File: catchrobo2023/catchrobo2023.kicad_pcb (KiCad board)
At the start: 2 copper layers, 72 x 47 mm, 38 parts, among them J1 Conn_01x03_Male, J2 Conn_01x03_Male, J3 Conn_01x03_Male, J4 Conn_01x02_Male, J5 Conn_01x02_Male, J6 Conn_01x02_Male, J7 Conn_01x02_Male, J8 Conn_01x02_Male, Q1 AO3401A, SW1 SW_SPDT, SW2 SW_DIP_x04, U11 SPT15, U2 RaspberryPiPicoW, U3 AZ1084-5.0, U4 LBR-127HLD, U5 LBR-127HLD, U6 LBR-127HLD, U7 LBR-127HLD, U8 CD4051BM96

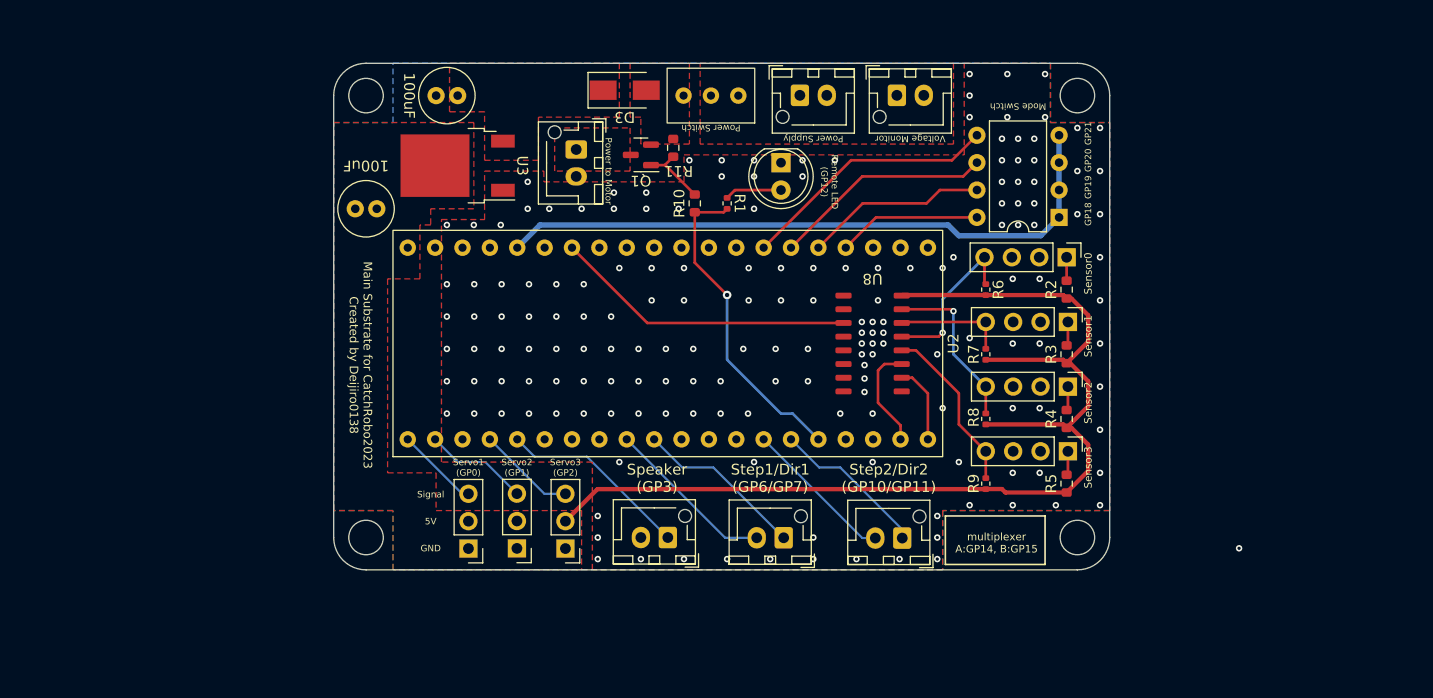
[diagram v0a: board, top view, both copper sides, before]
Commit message: 5V電源(XH)を追加
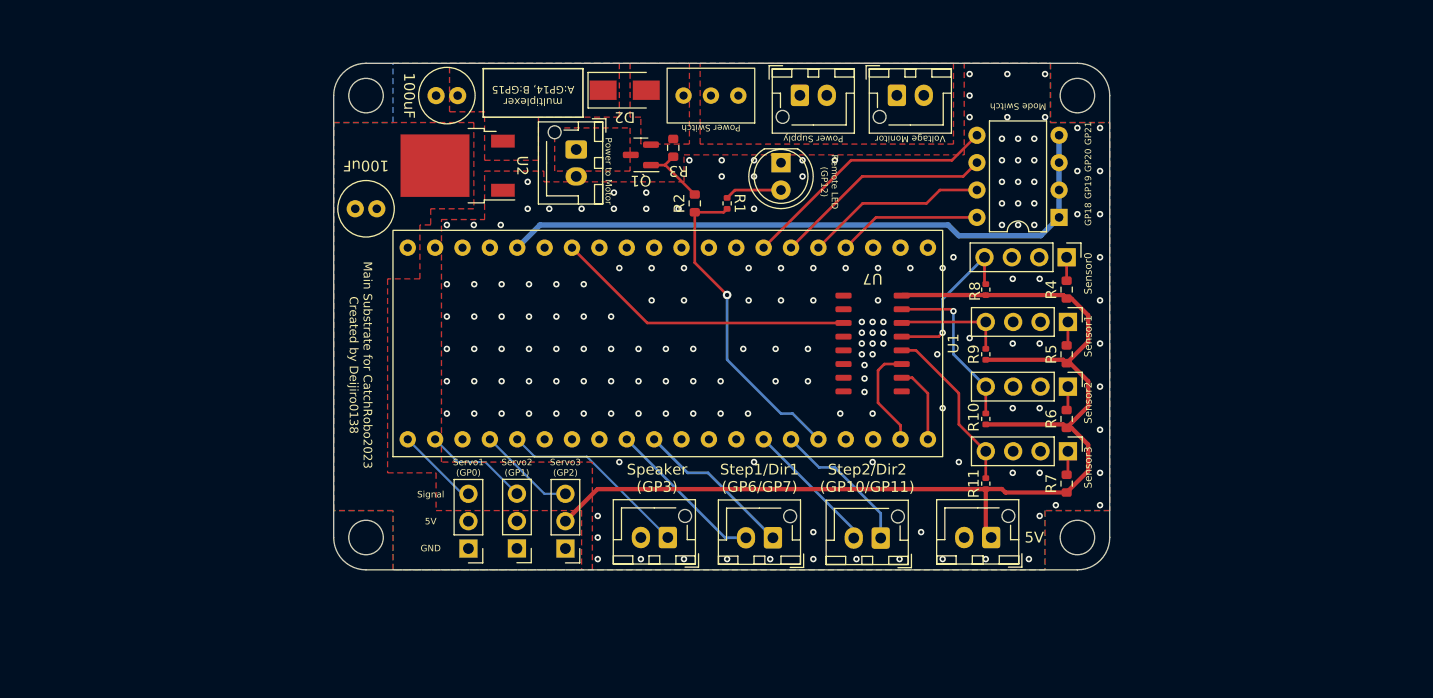
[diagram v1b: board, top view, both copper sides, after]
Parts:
- added J6: Conn_01x02_Male, Connector_JST:JST_XH_B2B-XH-AM_1x02_P2.50mm_Vertical, F.Cu at (141.0, 117.0)
- moved J5 2.00 mm to (130.8, 117.0)
- moved J4 1.00 mm to (120.8, 117.0)
- renumbered D2 to D1, D3 to D2, J4 to J1, J6 to J2, J7 to J3, J5 to J4, J8 to J5, J1 to J7, J2 to J8, J3 to J9, R8 to R10, R9 to R11, R10 to R2, R11 to R3, R2 to R4, R3 to R5, R4 to R6, R5 to R7, R6 to R8, R7 to R9, U2 to U1, U3 to U2, U4 to U3, U5 to U4, U6 to U5, U7 to U6, U8 to U7, U11 to U8
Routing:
- net +5V: track 102.3 -> 107.0 mm
- net /STEP2: track 14.2 -> 12.6 mm
- net /DIR2: track 14.6 -> 13.5 mm
- net /STEP1: track 15.8 -> 14.8 mm
- net /DIR1: track 15.8 -> 14.8 mm
- net (no net): vias 1 -> 0

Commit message: コントローラへの配線以外は完了
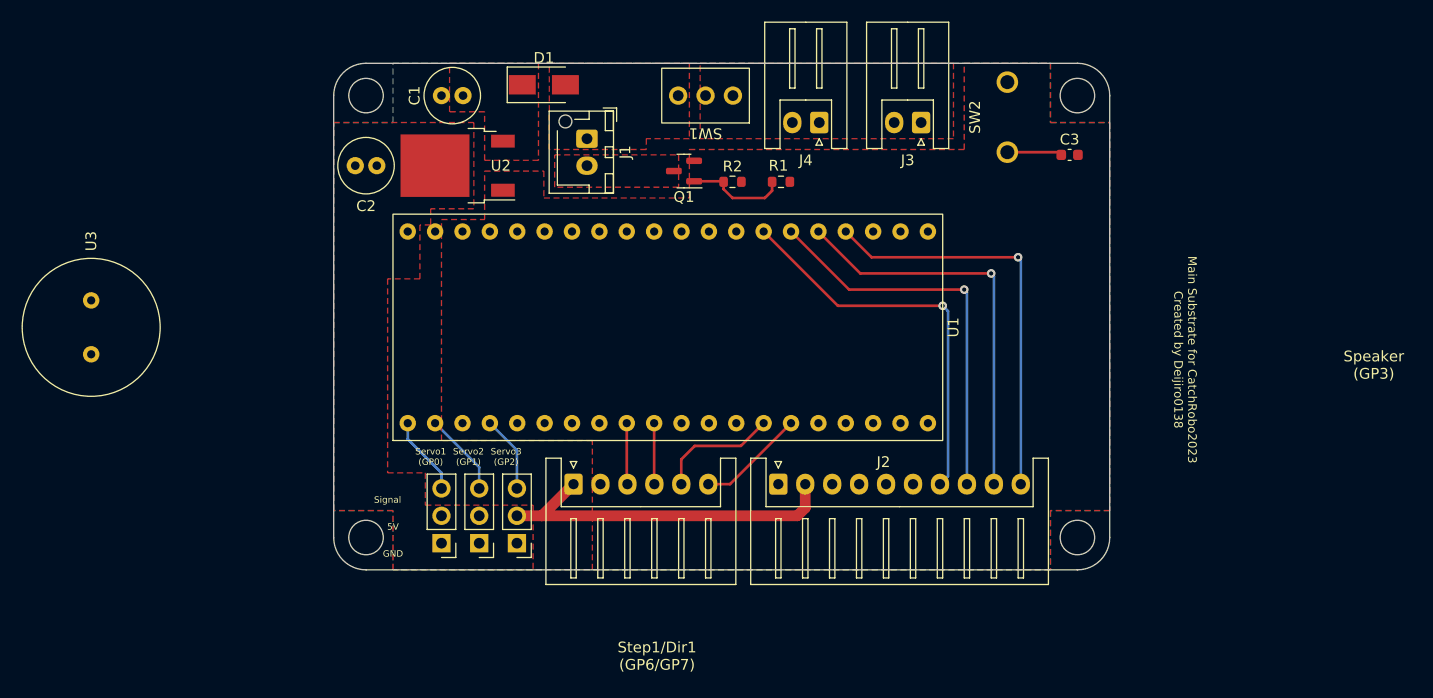
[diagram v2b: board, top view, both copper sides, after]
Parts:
- removed D2: D_Schottky, Diode_SMD:D_SMA
- removed J9: Conn_01x03_Male, Connector_PinHeader_2.54mm:PinHeader_1x03_P2.54mm_Vertical
- removed R10, R11, R8, R9: 1k, Resistor_SMD:R_0402_1005Metric
- removed R3: 10k, Resistor_SMD:R_0603_1608Metric
- removed R4, R5, R6, R7: 220, Resistor_SMD:R_0603_1608Metric
- removed U4, U5, U6: LBR-127HLD, Connector_PinHeader_2.54mm:PinHeader_1x04_P2.54mm_Vertical
- removed U7: CD4051BM96, Catchrobo_parts:SOIC-16-150mil
- removed U8: SPT15, Connector_JST:JST_XH_B2B-XH-AM_1x02_P2.50mm_Vertical
- added C3: 0.1u, Capacitor_SMD:C_0603_1608Metric, F.Cu at (148.3, 81.5)
- D1: value LED -> D_Schottky; footprint LED_THT:LED_D5.0mm -> Diode_SMD:D_SMA
- J2: value Conn_01x02_Male -> Conn_01x10_Male; footprint Connector_JST:JST_XH_B2B-XH-AM_1x02_P2.50mm_Vertical -> Connector_JST:JST_XH_S10B-XH-A_1x10_P2.50mm_Horizontal
- J3, J4: footprint Connector_JST:JST_XH_B2B-XH-AM_1x02_P2.50mm_Vertical -> Connector_JST:JST_XH_S2B-XH-A_1x02_P2.50mm_Horizontal
- J5: value Conn_01x02_Male -> Conn_01x06_Male; footprint Connector_JST:JST_XH_B2B-XH-AM_1x02_P2.50mm_Vertical -> Connector_JST:JST_XH_S6B-XH-A_1x06_P2.50mm_Horizontal
- J6: value Conn_01x02_Male -> Conn_01x03_Male; footprint Connector_JST:JST_XH_B2B-XH-AM_1x02_P2.50mm_Vertical -> Connector_PinHeader_2.54mm:PinHeader_1x03_P2.54mm_Vertical
- Q1: value AO3401A -> Q_NMOS_GSD
- R1: value 1k -> 330; footprint Resistor_SMD:R_0402_1005Metric -> Resistor_SMD:R_0603_1608Metric
- R2: value 330 -> 10k
- SW2: value SW_DIP_x04 -> SW_Push; footprint Package_DIP:DIP-8_W7.62mm -> Catchrobo_parts:TactSwitch
- U3: value LBR-127HLD -> SPT15; footprint Connector_PinHeader_2.54mm:PinHeader_1x04_P2.54mm_Vertical -> Catchrobo_parts:PKM13EPYH4000-A0
- moved U3 90.7 mm to (57.5, 97.5), turned to 90 degrees
- moved J6 51.0 mm to (90.0, 117.5)
- moved J4 38.8 mm to (125.0, 78.5)
- moved J2 36.1 mm to (121.2, 112.0)
- moved J5 28.9 mm to (102.2, 112.0), turned to 0 degrees
- moved D1 23.2 mm to (99.5, 75.0), turned to 0 degrees
- moved SW2 10.5 mm to (142.5, 78.0), turned to 90 degrees
- moved R1 5.39 mm to (121.5, 84.0), turned to 180 degrees
- moved Q1 4.27 mm to (112.5, 83.0)
- moved R2 4.03 mm to (117.0, 84.0), turned to 0 degrees
- moved C2 4.00 mm to (84.0, 82.5)
- moved J3 3.38 mm to (134.5, 78.5), turned to 180 degrees
- moved U1 1.50 mm to (111.0, 97.5)
- moved J1 1.41 mm to (103.5, 80.0)
- moved J7 1.12 mm to (93.5, 117.5)
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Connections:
- D1 pad 1: GND -> +7.5V
- J1 pad 1: Net-(J1-Pad1) -> Net-(D1-Pad2)
- J1 pad 2: GND -> Net-(J1-Pad2)
- J2 pad 1: +BATT -> GND
- J2 pad 2: GND -> +5V
- J4 pad 1: /DIR1 -> +BATT
- J4 pad 2: /STEP1 -> GND
- J5 pad 1: /DIR2 -> +5V
- J5 pad 2: /STEP2 -> GND
- J6 pad 1: +5V -> GND
- J6 pad 2: GND -> +5V
- J7 pad 3: /Servo1 -> /Servo2
- J8 pad 3: /Servo2 -> /Servo3
- Q1 pad 2: Net-(D2-Pad2) -> GND
- Q1 pad 3: Net-(J1-Pad1) -> Net-(J1-Pad2)
- R1 pad 1: Net-(D1-Pad2) -> /Stopper
- R1 pad 2: /Stopper -> Net-(Q1-Pad1)
- R2 pad 1: /Stopper -> Net-(Q1-Pad1)
- R2 pad 2: Net-(Q1-Pad1) -> GND
- SW1 pad 3: Net-(D2-Pad2) -> Net-(D1-Pad2)
- SW2 pad 1: +3.3V -> Net-(C3-Pad1)
- SW2 pad 2: +3.3V -> GND
- U1 pad 16: /Stopper -> unconnected-(U1-Pad16)
- U1 pad 19: /MultiA -> unconnected-(U1-Pad19)
- U1 pad 20: /MultiB -> unconnected-(U1-Pad20)
- U1 pad 24: /DIPSW0 -> /SW0
- U1 pad 25: /DIPSW1 -> /SW1
- U1 pad 26: /DIPSW2 -> /SW2
- U1 pad 27: /DIPSW3 -> /SW3
- U1 pad 30: unconnected-(U1-Pad30) -> Net-(C3-Pad1)
- U1 pad 31: unconnected-(U1-Pad31) -> /JoyX
- U1 pad 32: unconnected-(U1-Pad32) -> /JoyY
- U1 pad 34: /Sensor -> unconnected-(U1-Pad34)
- U3 pad 1: Net-(R4-Pad2) -> /Speaker
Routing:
- net +5V: track 107.0 -> 33.4 mm
- net +3.3V: track 59.9 -> 0.00 mm
- net /SW0: track 0.00 -> 38.1 mm, vias 0 -> 1
- net /SW1: track 0.00 -> 37.3 mm, vias 0 -> 1
- net /SW3: track 0.00 -> 36.5 mm, vias 0 -> 1
- net /SW2: track 0.00 -> 36.5 mm, vias 0 -> 1
- net /Stopper: track 29.6 -> 0.00 mm, vias 1 -> 0
- net /Sensor: track 28.1 -> 0.00 mm
- net /DIPSW3: track 24.1 -> 0.00 mm
- net /DIPSW2: track 20.5 -> 0.00 mm
- net /Speaker: track 17.7 -> 0.00 mm
- net /DIPSW1: track 16.9 -> 0.00 mm
- net /Sensor3: track 15.9 -> 0.00 mm
- net /Sensor2: track 15.6 -> 0.00 mm, vias 1 -> 0
- net /Sensor0: track 15.1 -> 0.00 mm, vias 1 -> 0
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- added copper zone on F.Cu, net Net-(D1-Pad2)
- added copper zone on F.Cu, net Net-(J1-Pad2)
- removed copper zone on F.Cu, net Net-(D2-Pad2)
- removed copper zone on F.Cu, net Net-(J1-Pad1)
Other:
- board text removed: "100uF"
- board text removed: "GP18"
- board text removed: "GP19"
- board text removed: "GP20"
- board text removed: "GP21"
- board text removed: "Mode Switch"
- board text removed: "Power Supply"
- board text removed: "Power Switch"
- board text removed: "Power to Motor"
- board text removed: "Remote LED (GP12)"
- board text removed: "Sensor0"
- board text removed: "Sensor1"
- board text removed: "Sensor2"
- board text removed: "Sensor3"
- board text removed: "Step2/Dir2 (GP10/GP11)"
- board text removed: "Voltage Monitor"
- board text removed: "multiplexer A:GP14, B:GP15"

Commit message: Main基板の修正完了
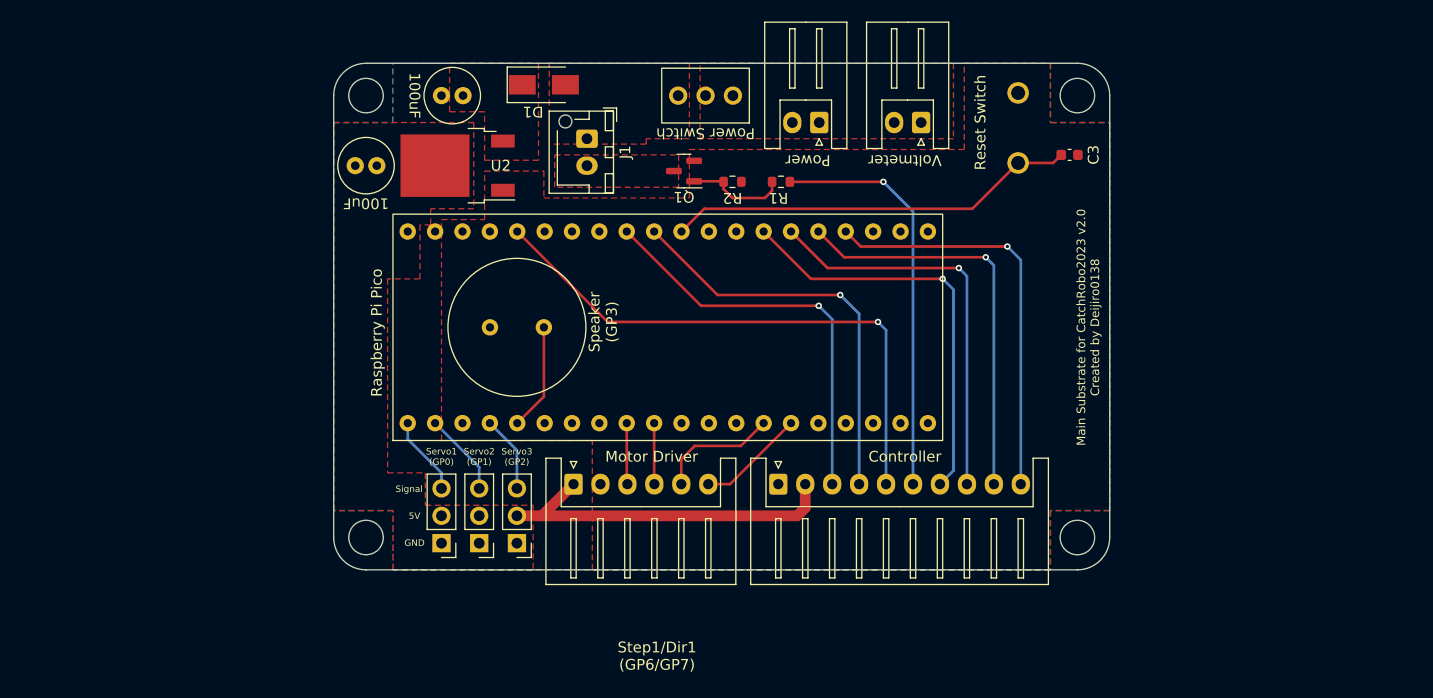
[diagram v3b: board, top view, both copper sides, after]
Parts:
- moved U3 39.5 mm to (97.0, 97.5), turned to 180 degrees
- moved SW2 1.41 mm to (143.5, 79.0)
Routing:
- net +3.3V: track 0.00 -> 52.3 mm, vias 0 -> 1
- net /JoyX: track 0.00 -> 38.0 mm, vias 0 -> 1
- net /Stopper: track 0.00 -> 37.9 mm, vias 0 -> 1
- net /JoyY: track 0.00 -> 37.7 mm, vias 0 -> 1
- net Net-(C3-Pad1): track 5.10 -> 38.5 mm
- net /Speaker: track 0.00 -> 9.91 mm
- net /SW3: track 36.5 -> 38.4 mm
- net /SW2: track 36.5 -> 37.3 mm
- net /SW1: track 37.3 -> 37.9 mm
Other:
- board text added: "100uF"
- board text added: "Controller"
- board text added: "Main Substrate for CatchRobo2023 v2.0 Created by Deijiro0138"
- board text added: "Motor Driver"
- board text added: "Power"
- board text added: "Power Switch"
- board text added: "Raspberry Pi Pico"
- board text added: "Reset Switch"
- board text added: "Voltmeter"
- board text removed: "Main Substrate for CatchRobo2023 Created by Deijiro0138"

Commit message: MDを修正
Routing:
- net GND: vias 0 -> 110
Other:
- board text removed: "Step1/Dir1 (GP6/GP7)"
